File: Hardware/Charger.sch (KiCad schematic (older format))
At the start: 0 parts

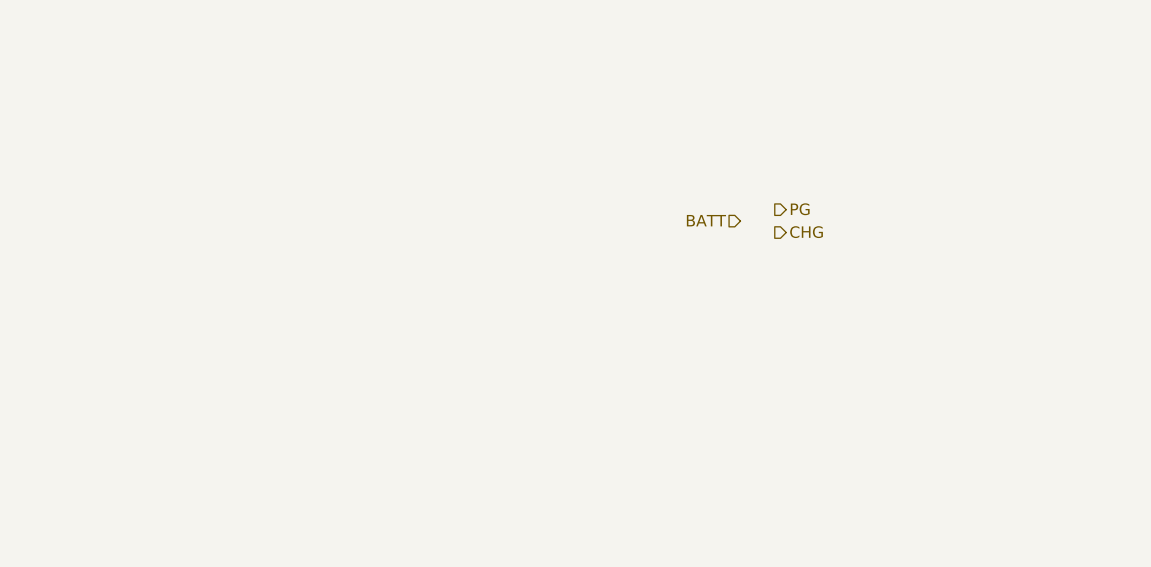
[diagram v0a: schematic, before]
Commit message: Battery charger IC added
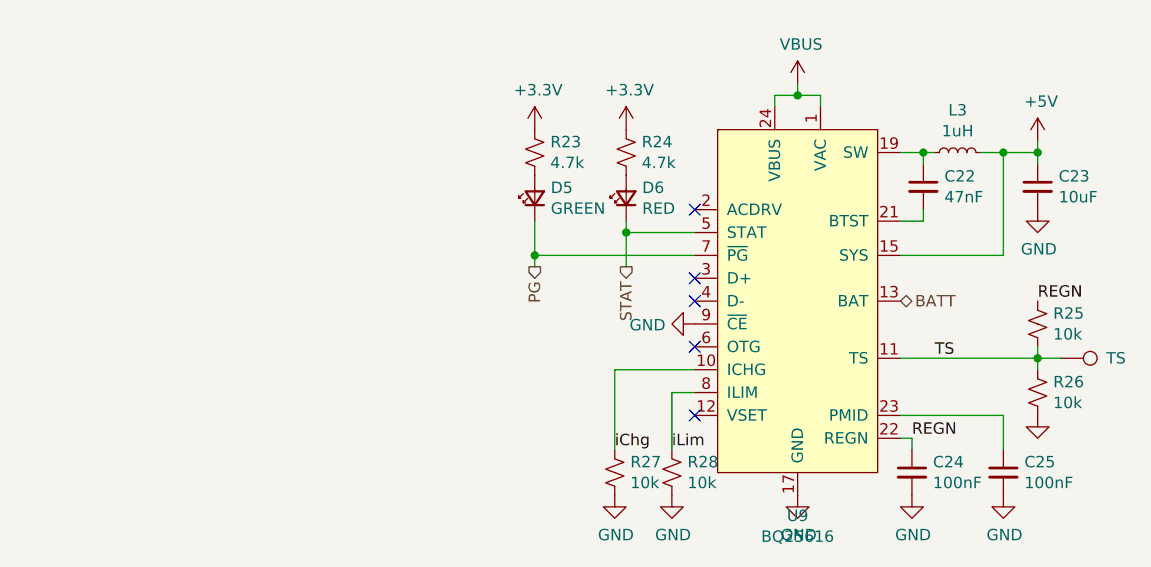
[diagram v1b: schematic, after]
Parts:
- added C22: 47nF, Capacitor_SMD:C_0402_1005Metric, symbol Device:C_Small
- added C23: 10uF, Capacitor_SMD:C_0603_1608Metric, symbol Device:C_Small
- added C24, C25: 100nF, Capacitor_SMD:C_0402_1005Metric, symbol Device:C_Small
- added D5: GREEN, LED_SMD:LED_0402_1005Metric, symbol Device:LED_Small
- added D6: RED, LED_SMD:LED_0402_1005Metric, symbol Device:LED_Small
- added L3: 1uH, Inductor_SMD:L_1210_3225Metric, symbol Device:L_Small
- added R23, R24: 4.7k, Resistor_SMD:R_0402_1005Metric, symbol Device:R_Small_US
- added R25, R26, R27, R28: 10k, Resistor_SMD:R_0402_1005Metric, symbol Device:R_Small_US
- added TP2: TS, TestPoint:TestPoint_Pad_1.0x1.0mm, symbol Connector:TestPoint
- added U9: BQ25616, Package_DFN_QFN:WQFN-24-1EP_4x4mm_P0.5mm_EP2.6x2.6mm_ThermalVias, symbol bq25616:BQ25616
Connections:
- net BATT: now also U9.13 (BAT), U9.14 (BAT)
- net PG: now also D5.1 (K), U9.7 (~PG)
- new net: C25.1, U9.23 (PMID)
- new net: C22.1, L3.1, U9.19 (SW), U9.20 (SW)
- new net: C22.2, U9.21 (BTST)
- new net: D6.2 (A), R24.2
- new net: D5.2 (A), R23.2
- new net +3V3: R23.1, R24.1
- new net +5V: C23.1, L3.2, U9.15 (SYS), U9.16 (SYS)
- new net GND: C23.2, C24.2, C25.2, R26.2, R27.2, R28.2, U9.17 (GND), U9.18 (GND), U9.25 (GND), U9.9 (~CE)
- new net REGN: C24.1, R25.1, U9.22 (REGN)
- new net STAT: D6.1 (K), U9.5 (STAT)
- new net TS: R25.2, R26.1, TP2.1, U9.11 (TS)
- new net VBUS: U9.1 (VAC), U9.24 (VBUS)
- new net iChg: R27.1, U9.10 (ICHG)
- new net iLim: R28.1, U9.8 (ILIM)
- no-connect marks 0 -> 5

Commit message: Net names declared in root sheet
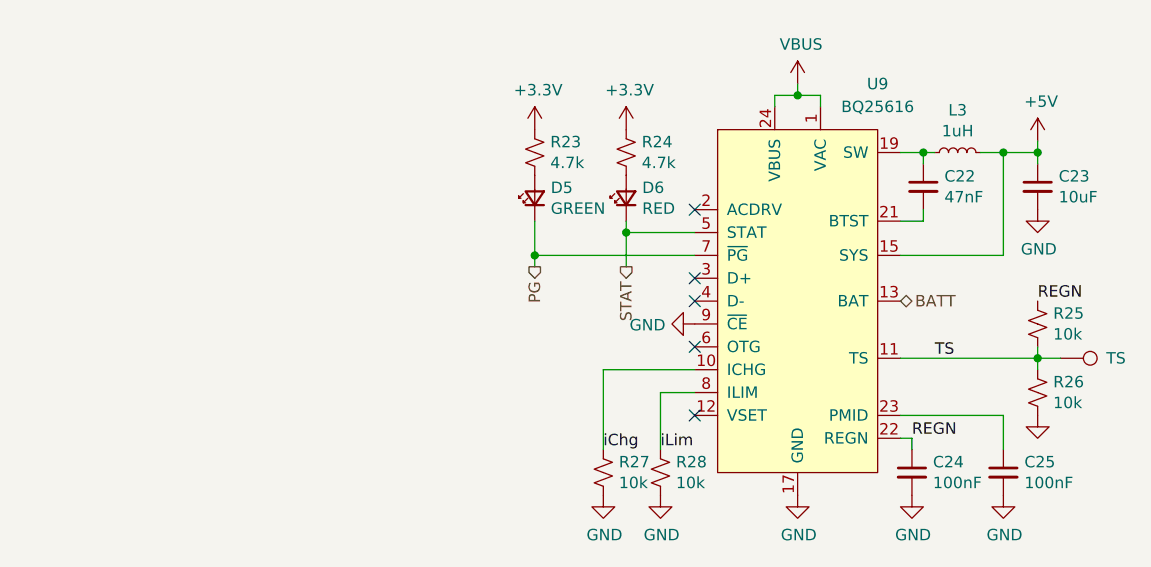
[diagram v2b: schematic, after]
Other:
- moved on the sheet: R27, R28

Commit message: Replaced ESP-WROOM-32D with ESP32-CAM
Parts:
- renumbered C22 to C12, C23 to C13, C24 to C14, C25 to C15, D5 to D1, D6 to D2, L3 to L1, R23 to R17, R24 to R18, R25 to R19, R26 to R20, R27 to R21, R28 to R22, U9 to U7
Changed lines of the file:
@@
 AR Path="/600FC875/5FEF1028" Ref="R?"  Part="1"
 AR Path="/5FF0711D/5FEEEAE7/5FEF1028" Ref="R?"  Part="1"
-AR Path="/5FF0711D/5FEF1028" Ref="R28"  Part="1"
-F 0 "R28" H 5168 4796 50  0000 L CNN
+AR Path="/5FF0711D/5FEF1028" Ref="R22"  Part="1"
+F 0 "R22" H 5168 4796 50  0000 L CNN
 F 1 "10k" H 5168 4705 50  0000 L CNN
 F 2 "Resistor_SMD:R_0402_1005Metric" H 5100 4750 50  0001 C CNN
@@
 AR Path="/600FC875/5FEF102E" Ref="R?"  Part="1"
 AR Path="/5FF0711D/5FEEEAE7/5FEF102E" Ref="R?"  Part="1"
-AR Path="/5FF0711D/5FEF102E" Ref="R27"  Part="1"
-F 0 "R27" H 4918 4796 50  0000 L CNN
+AR Path="/5FF0711D/5FEF102E" Ref="R21"  Part="1"
+F 0 "R21" H 4918 4796 50  0000 L CNN
 F 1 "10k" H 4918 4705 50  0000 L CNN
 F 2 "Resistor_SMD:R_0402_1005Metric" H 4850 4750 50  0001 C CNN
@@
 AR Path="/600FC875/5FEF105A" Ref="C?"  Part="1"
 AR Path="/5FF0711D/5FEEEAE7/5FEF105A" Ref="C?"  Part="1"
-AR Path="/5FF0711D/5FEF105A" Ref="C25"  Part="1"
-F 0 "C25" H 6692 4796 50  0000 L CNN
+AR Path="/5FF0711D/5FEF105A" Ref="C15"  Part="1"
+F 0 "C15" H 6692 4796 50  0000 L CNN
 F 1 "100nF" H 6692 4705 50  0000 L CNN
 F 2 "Capacitor_SMD:C_0402_1005Metric" H 6600 4750 50  0001 C CNN
@@
 AR Path="/600FC875/5FEF1060" Ref="C?"  Part="1"
 AR Path="/5FF0711D/5FEEEAE7/5FEF1060" Ref="C?"  Part="1"
-AR Path="/5FF0711D/5FEF1060" Ref="C24"  Part="1"
-F 0 "C24" H 6292 4796 50  0000 L CNN
+AR Path="/5FF0711D/5FEF1060" Ref="C14"  Part="1"
+F 0 "C14" H 6292 4796 50  0000 L CNN
 F 1 "100nF" H 6292 4705 50  0000 L CNN
 F 2 "Capacitor_SMD:C_0402_1005Metric" H 6200 4750 50  0001 C CNN
@@
 AR Path="/600FC875/5FEF1066" Ref="R?"  Part="1"
 AR Path="/5FF0711D/5FEEEAE7/5FEF1066" Ref="R?"  Part="1"
-AR Path="/5FF0711D/5FEF1066" Ref="R25"  Part="1"
-F 0 "R25" H 6818 4146 50  0000 L CNN
+AR Path="/5FF0711D/5FEF1066" Ref="R19"  Part="1"
+F 0 "R19" H 6818 4146 50  0000 L CNN
 F 1 "10k" H 6818 4055 50  0000 L CNN
 F 2 "Resistor_SMD:R_0402_1005Metric" H 6750 4100 50  0001 C CNN
@@
 AR Path="/600FC875/5FEF106C" Ref="R?"  Part="1"
 AR Path="/5FF0711D/5FEEEAE7/5FEF106C" Ref="R?"  Part="1"
-AR Path="/5FF0711D/5FEF106C" Ref="R26"  Part="1"
-F 0 "R26" H 6818 4446 50  0000 L CNN
+AR Path="/5FF0711D/5FEF106C" Ref="R20"  Part="1"
+F 0 "R20" H 6818 4446 50  0000 L CNN
 F 1 "10k" H 6818 4355 50  0000 L CNN
 F 2 "Resistor_SMD:R_0402_1005Metric" H 6750 4400 50  0001 C CNN
@@
 AR Path="/600FC875/5FEF1085" Ref="C?"  Part="1"
 AR Path="/5FF0711D/5FEEEAE7/5FEF1085" Ref="C?"  Part="1"
-AR Path="/5FF0711D/5FEF1085" Ref="C22"  Part="1"
-F 0 "C22" H 6342 3546 50  0000 L CNN
+AR Path="/5FF0711D/5FEF1085" Ref="C12"  Part="1"
+F 0 "C12" H 6342 3546 50  0000 L CNN
 F 1 "47nF" H 6342 3455 50  0000 L CNN
 F 2 "Capacitor_SMD:C_0402_1005Metric" H 6250 3500 50  0001 C CNN
@@
 AR Path="/600FC875/5FEF1090" Ref="L?"  Part="1"
 AR Path="/5FF0711D/5FEEEAE7/5FEF1090" Ref="L?"  Part="1"
-AR Path="/5FF0711D/5FEF1090" Ref="L3"  Part="1"
-F 0 "L3" V 6585 3350 50  0000 C CNN
+AR Path="/5FF0711D/5FEF1090" Ref="L1"  Part="1"
+F 0 "L1" V 6585 3350 50  0000 C CNN
 F 1 "1uH" V 6494 3350 50  0000 C CNN
 F 2 "Inductor_SMD:L_1210_3225Metric" H 6400 3350 50  0001 C CNN
@@
 AR Path="/600FC875/5FEF1098" Ref="C?"  Part="1"
 AR Path="/5FF0711D/5FEEEAE7/5FEF1098" Ref="C?"  Part="1"
-AR Path="/5FF0711D/5FEF1098" Ref="C23"  Part="1"
-F 0 "C23" H 6842 3546 50  0000 L CNN
+AR Path="/5FF0711D/5FEF1098" Ref="C13"  Part="1"
+F 0 "C13" H 6842 3546 50  0000 L CNN
 F 1 "10uF" H 6842 3455 50  0000 L CNN
 F 2 "Capacitor_SMD:C_0603_1608Metric" H 6750 3500 50  0001 C CNN
@@
 AR Path="/600FC875/5FEF10BE" Ref="R?"  Part="1"
 AR Path="/5FF0711D/5FEEEAE7/5FEF10BE" Ref="R?"  Part="1"
-AR Path="/5FF0711D/5FEF10BE" Ref="R24"  Part="1"
-F 0 "R24" H 5018 3396 50  0000 L CNN
+AR Path="/5FF0711D/5FEF10BE" Ref="R18"  Part="1"
+F 0 "R18" H 5018 3396 50  0000 L CNN
 F 1 "4.7k" H 5018 3305 50  0000 L CNN
 F 2 "Resistor_SMD:R_0402_1005Metric" H 4950 3350 50  0001 C CNN
@@
 AR Path="/600FC875/5FEF10CB" Ref="D?"  Part="1"
 AR Path="/5FF0711D/5FEEEAE7/5FEF10CB" Ref="D?"  Part="1"
-AR Path="/5FF0711D/5FEF10CB" Ref="D6"  Part="1"
-F 0 "D6" V 4996 3480 50  0000 R CNN
+AR Path="/5FF0711D/5FEF10CB" Ref="D2"  Part="1"
+F 0 "D2" V 4996 3480 50  0000 R CNN
 F 1 "RED" V 4905 3480 50  0000 R CNN
 F 2 "LED_SMD:LED_0402_1005Metric" V 4950 3550 50  0001 C CNN
@@
 AR Path="/600FC875/5FEF10D2" Ref="R?"  Part="1"
 AR Path="/5FF0711D/5FEEEAE7/5FEF10D2" Ref="R?"  Part="1"
-AR Path="/5FF0711D/5FEF10D2" Ref="R23"  Part="1"
-F 0 "R23" H 4618 3396 50  0000 L CNN
+AR Path="/5FF0711D/5FEF10D2" Ref="R17"  Part="1"
+F 0 "R17" H 4618 3396 50  0000 L CNN
 F 1 "4.7k" H 4618 3305 50  0000 L CNN
 F 2 "Resistor_SMD:R_0402_1005Metric" H 4550 3350 50  0001 C CNN
@@
 AR Path="/600FC875/5FEF10DE" Ref="D?"  Part="1"
 AR Path="/5FF0711D/5FEEEAE7/5FEF10DE" Ref="D?"  Part="1"
-AR Path="/5FF0711D/5FEF10DE" Ref="D5"  Part="1"
-F 0 "D5" V 4596 3480 50  0000 R CNN
+AR Path="/5FF0711D/5FEF10DE" Ref="D1"  Part="1"
+F 0 "D1" V 4596 3480 50  0000 R CNN
 F 1 "GREEN" V 4505 3480 50  0000 R CNN
 F 2 "LED_SMD:LED_0402_1005Metric" V 4550 3550 50  0001 C CNN
@@
 iLim
 $Comp
-L bq25616:BQ25616 U9
+L bq25616:BQ25616 U7
 U 1 1 5FEF3DC6
 P 5700 3950
-F 0 "U9" H 6050 4850 50  0000 C CNN
+F 0 "U7" H 6050 4850 50  0000 C CNN
 F 1 "BQ25616" H 6050 4750 50  0000 C CNN
 F 2 "Package_DFN_QFN:WQFN-24-1EP_4x4mm_P0.5mm_EP2.6x2.6mm_ThermalVias" H 6050 4850 50  0001 C CNN

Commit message: Signed-off-by: Usman <usmanmehmood55@gmail.com>
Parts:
- added J?: USB_C_Receptacle_USB2.0, symbol Connector:USB_C_Receptacle_USB2.0
- renumbered R17 to R19, R18 to R20, R19 to R21, R20 to R22, R21 to R23, R22 to R24
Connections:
- new net: J?.A1 (GND), J?.A12 (GND), J?.B1 (GND), J?.B12 (GND)
- new net: J?.A4 (VBUS), J?.A9 (VBUS), J?.B4 (VBUS), J?.B9 (VBUS)
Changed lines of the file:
@@
 AR Path="/600FC875/5FEF1028" Ref="R?"  Part="1"
 AR Path="/5FF0711D/5FEEEAE7/5FEF1028" Ref="R?"  Part="1"
-AR Path="/5FF0711D/5FEF1028" Ref="R22"  Part="1"
-F 0 "R22" H 5168 4796 50  0000 L CNN
+AR Path="/5FF0711D/5FEF1028" Ref="R24"  Part="1"
+F 0 "R24" H 5168 4796 50  0000 L CNN
 F 1 "10k" H 5168 4705 50  0000 L CNN
 F 2 "Resistor_SMD:R_0402_1005Metric" H 5100 4750 50  0001 C CNN
@@
 AR Path="/600FC875/5FEF102E" Ref="R?"  Part="1"
 AR Path="/5FF0711D/5FEEEAE7/5FEF102E" Ref="R?"  Part="1"
-AR Path="/5FF0711D/5FEF102E" Ref="R21"  Part="1"
-F 0 "R21" H 4918 4796 50  0000 L CNN
+AR Path="/5FF0711D/5FEF102E" Ref="R23"  Part="1"
+F 0 "R23" H 4918 4796 50  0000 L CNN
 F 1 "10k" H 4918 4705 50  0000 L CNN
 F 2 "Resistor_SMD:R_0402_1005Metric" H 4850 4750 50  0001 C CNN
@@
 AR Path="/600FC875/5FEF1066" Ref="R?"  Part="1"
 AR Path="/5FF0711D/5FEEEAE7/5FEF1066" Ref="R?"  Part="1"
-AR Path="/5FF0711D/5FEF1066" Ref="R19"  Part="1"
-F 0 "R19" H 6818 4146 50  0000 L CNN
+AR Path="/5FF0711D/5FEF1066" Ref="R21"  Part="1"
+F 0 "R21" H 6818 4146 50  0000 L CNN
 F 1 "10k" H 6818 4055 50  0000 L CNN
 F 2 "Resistor_SMD:R_0402_1005Metric" H 6750 4100 50  0001 C CNN
@@
 AR Path="/600FC875/5FEF106C" Ref="R?"  Part="1"
 AR Path="/5FF0711D/5FEEEAE7/5FEF106C" Ref="R?"  Part="1"
-AR Path="/5FF0711D/5FEF106C" Ref="R20"  Part="1"
-F 0 "R20" H 6818 4446 50  0000 L CNN
+AR Path="/5FF0711D/5FEF106C" Ref="R22"  Part="1"
+F 0 "R22" H 6818 4446 50  0000 L CNN
 F 1 "10k" H 6818 4355 50  0000 L CNN
 F 2 "Resistor_SMD:R_0402_1005Metric" H 6750 4400 50  0001 C CNN
@@
 AR Path="/600FC875/5FEF10BE" Ref="R?"  Part="1"
 AR Path="/5FF0711D/5FEEEAE7/5FEF10BE" Ref="R?"  Part="1"
-AR Path="/5FF0711D/5FEF10BE" Ref="R18"  Part="1"
-F 0 "R18" H 5018 3396 50  0000 L CNN
+AR Path="/5FF0711D/5FEF10BE" Ref="R20"  Part="1"
+F 0 "R20" H 5018 3396 50  0000 L CNN
 F 1 "4.7k" H 5018 3305 50  0000 L CNN
 F 2 "Resistor_SMD:R_0402_1005Metric" H 4950 3350 50  0001 C CNN
@@
 AR Path="/600FC875/5FEF10D2" Ref="R?"  Part="1"
 AR Path="/5FF0711D/5FEEEAE7/5FEF10D2" Ref="R?"  Part="1"
-AR Path="/5FF0711D/5FEF10D2" Ref="R17"  Part="1"
-F 0 "R17" H 4618 3396 50  0000 L CNN
+AR Path="/5FF0711D/5FEF10D2" Ref="R19"  Part="1"
+F 0 "R19" H 4618 3396 50  0000 L CNN
 F 1 "4.7k" H 4618 3305 50  0000 L CNN
 F 2 "Resistor_SMD:R_0402_1005Metric" H 4550 3350 50  0001 C CNN
@@
 Wire Wire Line
 	4850 4300 5250 4300
+$Comp
+L Connector:USB_C_Receptacle_USB2.0 J?
+U 1 1 60721A3E
+P 2750 4100
+F 0 "J?" H 2857 4967 50  0000 C CNN
+F 1 "USB_C_Receptacle_USB2.0" H 2857 4876 50  0000 C CNN
+F 2 "" H 2900 4100 50  0001 C CNN
+F 3 "https://www.usb.org/sites/default/files/documents/usb_type-c.zip" H 2900 4100 50  0001 C CNN
+	1    2750 4100
+	1    0    0    -1
+$EndComp
 $EndSCHEMATC

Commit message: Schematic updated, USB comms circuit added
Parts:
- removed J?: USB_C_Receptacle_USB2.0, symbol Connector:USB_C_Receptacle_USB2.0
- C12, C14, C15: footprint Capacitor_SMD:C_0402_1005Metric -> Capacitor_SMD:C_0805_2012Metric
- C13: footprint Capacitor_SMD:C_0603_1608Metric -> Capacitor_SMD:C_0805_2012Metric
- R23: renamed from R19; footprint Resistor_SMD:R_0402_1005Metric -> Resistor_SMD:R_0805_2012Metric
- R24: renamed from R20; footprint Resistor_SMD:R_0402_1005Metric -> Resistor_SMD:R_0805_2012Metric
- R25: renamed from R21; footprint Resistor_SMD:R_0402_1005Metric -> Resistor_SMD:R_0805_2012Metric
- R26: renamed from R22; footprint Resistor_SMD:R_0402_1005Metric -> Resistor_SMD:R_0805_2012Metric
- R27: renamed from R23; footprint Resistor_SMD:R_0402_1005Metric -> Resistor_SMD:R_0805_2012Metric
- R28: renamed from R24; footprint Resistor_SMD:R_0402_1005Metric -> Resistor_SMD:R_0805_2012Metric
- renumbered TP2 to TP4, U7 to U8

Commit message: vbus connected from USB to charger sheet
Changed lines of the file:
@@
 	6750 3300 6750 3350
 Connection ~ 6750 3350
-$Comp
-L power:VBUS #PWR?
-U 1 1 5FEF10B2
-P 5700 3050
-AR Path="/5FEF10B2" Ref="#PWR?"  Part="1"
-AR Path="/600FC875/5FEF10B2" Ref="#PWR?"  Part="1"
-AR Path="/5FF0711D/5FEEEAE7/5FEF10B2" Ref="#PWR?"  Part="1"
-AR Path="/5FF0711D/5FEF10B2" Ref="#PWR051"  Part="1"
-F 0 "#PWR051" H 5700 2900 50  0001 C CNN
-F 1 "VBUS" H 5715 3223 50  0000 C CNN
-F 2 "" H 5700 3050 50  0001 C CNN
-F 3 "" H 5700 3050 50  0001 C CNN
-	1    5700 3050
-	1    0    0    -1
-$EndComp
 Wire Wire Line
 	5700 3050 5700 3100
@@
 Wire Wire Line
 	4850 4300 5250 4300
+Text HLabel 5700 3050 1    50   Input ~ 0
+VBUS
 $EndSCHEMATC

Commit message: PCB design started
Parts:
- C12: renamed from C14; symbol Device:C_Small -> Roverette-rescue:C_Small-Device
- C13: renamed from C12; symbol Device:C_Small -> Roverette-rescue:C_Small-Device
- C14: renamed from C15; symbol Device:C_Small -> Roverette-rescue:C_Small-Device
- C15: renamed from C13; symbol Device:C_Small -> Roverette-rescue:C_Small-Device
- D1, D2: symbol Device:LED_Small -> Roverette-rescue:LED_Small-Device
- L1: symbol Device:L_Small -> Roverette-rescue:L_Small-Device
- R23: symbol Device:R_Small_US -> Roverette-rescue:R_Small_US-Device
- R24: renamed from R27; symbol Device:R_Small_US -> Roverette-rescue:R_Small_US-Device
- R25: renamed from R24; symbol Device:R_Small_US -> Roverette-rescue:R_Small_US-Device
- R26: renamed from R28; symbol Device:R_Small_US -> Roverette-rescue:R_Small_US-Device
- R27: renamed from R25; symbol Device:R_Small_US -> Roverette-rescue:R_Small_US-Device
- R28: renamed from R26; symbol Device:R_Small_US -> Roverette-rescue:R_Small_US-Device
- TP4: symbol Connector:TestPoint -> Roverette-rescue:TestPoint-Connector
- renumbered U8 to U6
